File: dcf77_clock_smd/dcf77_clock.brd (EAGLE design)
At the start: 83.5 x 76.2 mm, 42 parts, among them IC1 7805DT, IC2 ATMEGA48/88/168-AU, J2 DCJ0202, Q2 IRLML6244TRPBF, SW1 EC12E_SW, U1 LCD-16X2SILK, U2 DS1307SO8

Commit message: ERC fixes
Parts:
- LED1: value (none) -> BLUE
- Q1: value (none) -> 32.768kHz
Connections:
- removed net N$8: IC2.14
- net LCD_DB6: now also IC2.11; no longer IC2.9
- net LCD_DB7: now also IC2.9; no longer IC2.11
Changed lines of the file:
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@@
 <attribute name="VALUE" x="73.914" y="75.692" size="1.27" layer="27" rot="R270"/>
 </element>
-<element name="LED1" library="led" library_urn="urn:adsk.eagle:library:259" package="CHIP-LED0805" package3d_urn="urn:adsk.eagle:package:15818/2" value="" x="55.88" y="41.91" smashed="yes" rot="R90">
+<element name="LED1" library="led" library_urn="urn:adsk.eagle:library:259" package="CHIP-LED0805" package3d_urn="urn:adsk.eagle:package:15818/2" value="BLUE" x="55.88" y="41.91" smashed="yes" rot="R90">
 <attribute name="NAME" x="55.499" y="43.815" size="1.27" layer="25" ratio="10" rot="R90"/>
 <attribute name="POPULARITY" value="68" x="55.88" y="41.91" size="1.778" layer="27" rot="R90" display="off"/>
@@
 <attribute name="NAME" x="23.45" y="76.5" size="1.27" layer="25"/>
 </element>
-<element name="Q1" library="crystal" library_urn="urn:adsk.eagle:library:204" package="MM39SL" package3d_urn="urn:adsk.eagle:package:12090/1" value="" x="30.48" y="58.42" smashed="yes">
+<element name="Q1" library="crystal" library_urn="urn:adsk.eagle:library:204" package="MM39SL" package3d_urn="urn:adsk.eagle:package:12090/1" value="32.768kHz" x="30.48" y="58.42" smashed="yes">
 <attribute name="MF" value="" x="30.48" y="58.42" size="1.778" layer="27" display="off"/>
 <attribute name="MPN" value="" x="30.48" y="58.42" size="1.778" layer="27" display="off"/>
@@
 <wire x1="41.1226" y1="46.45" x2="47.31" y2="60.96" width="0" layer="19" extent="1-1"/>
 </signal>
-<signal name="N$8">
-<contactref element="IC2" pad="14"/>
-</signal>
 <signal name="ISP_MISO">
 <contactref element="IC2" pad="16"/>
@@
 <signal name="LCD_DB6">
 <contactref element="U1" pad="13"/>
-<contactref element="IC2" pad="9"/>
-<wire x1="40.009" y1="35.058" x2="41.1226" y2="41.65" width="0" layer="19" extent="1-1"/>
+<contactref element="IC2" pad="11"/>
+<wire x1="40.009" y1="35.058" x2="41.1226" y2="43.25" width="0" layer="19" extent="1-1"/>
 </signal>
 <signal name="LCD_DB7">
 <contactref element="U1" pad="14"/>
-<contactref element="IC2" pad="11"/>
-<wire x1="42.549" y1="35.058" x2="41.1226" y2="43.25" width="0" layer="19" extent="1-1"/>
+<contactref element="IC2" pad="9"/>
+<wire x1="42.549" y1="35.058" x2="41.1226" y2="41.65" width="0" layer="19" extent="1-1"/>
 </signal>
 <signal name="N$9">

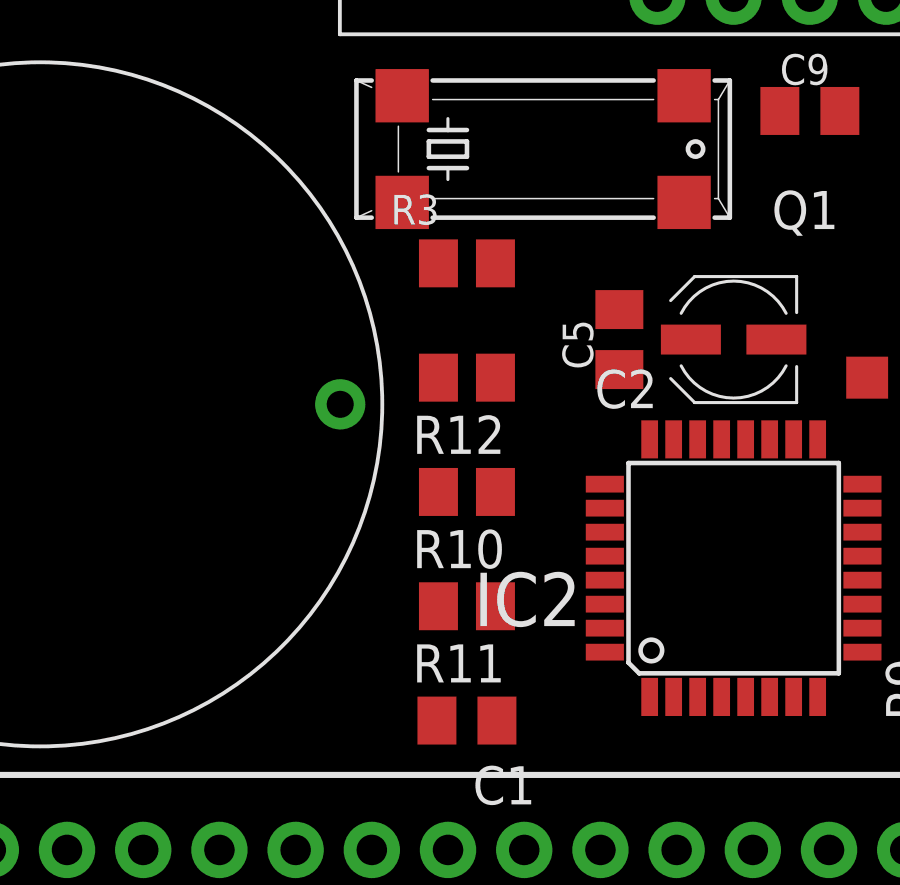
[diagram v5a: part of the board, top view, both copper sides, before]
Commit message: Rearrange I2C pullups
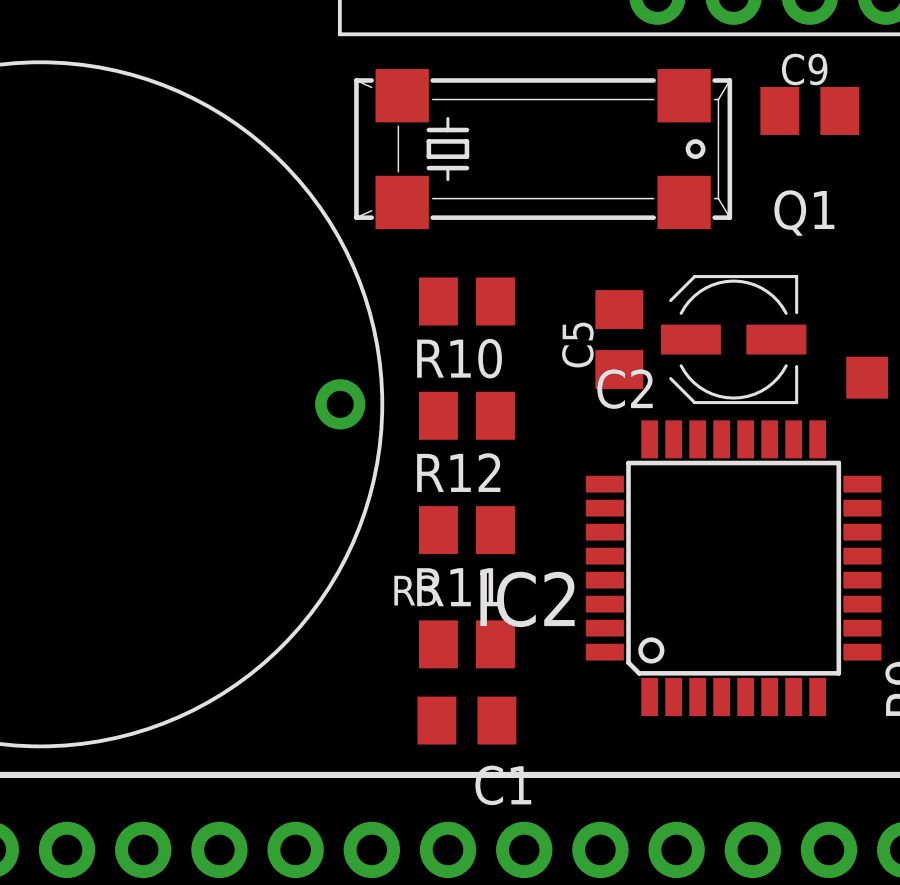
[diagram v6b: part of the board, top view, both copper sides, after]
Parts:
- moved R3 12.7 mm to (27.9, 41.9)
- moved R10 6.35 mm to (27.9, 53.3)
- moved R11 2.54 mm to (27.9, 45.7)
- moved R12 1.27 mm to (27.9, 49.5)
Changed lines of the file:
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@@
 <attribute name="VALUE" x="75.565" y="41.91" size="0.6096" layer="27" rot="R180"/>
 </element>
-<element name="R3" library="rcl" library_urn="urn:adsk.eagle:library:334" package="M0805" package3d_urn="urn:adsk.eagle:package:23556/2" value="10k" x="27.94" y="54.61" smashed="yes">
-<attribute name="NAME" x="25.4" y="55.9054" size="0.9906" layer="25" ratio="10"/>
-<attribute name="POPULARITY" value="45" x="27.94" y="54.61" size="1.778" layer="27" display="off"/>
-<attribute name="SPICEPREFIX" value="R" x="27.94" y="54.61" size="1.778" layer="27" display="off"/>
-<attribute name="VALUE" x="26.3144" y="54.1274" size="0.9906" layer="27" ratio="10"/>
+<element name="R3" library="rcl" library_urn="urn:adsk.eagle:library:334" package="M0805" package3d_urn="urn:adsk.eagle:package:23556/2" value="10k" x="27.94" y="41.91" smashed="yes">
+<attribute name="NAME" x="25.4" y="43.2054" size="0.9906" layer="25" ratio="10"/>
+<attribute name="POPULARITY" value="45" x="27.94" y="41.91" size="1.778" layer="27" display="off"/>
+<attribute name="SPICEPREFIX" value="R" x="27.94" y="41.91" size="1.778" layer="27" display="off"/>
+<attribute name="VALUE" x="26.3144" y="41.4274" size="0.9906" layer="27" ratio="10"/>
 </element>
 <element name="SG2" library="SparkFun" package="BUZZER-CCV-KIT" value="LD-BZEN-1201" x="49.53" y="45.72" smashed="yes">
@@
 <attribute name="VALUE" x="46.99" y="39.37" size="1.27" layer="27" rot="R90"/>
 </element>
-<element name="R10" library="rcl" library_urn="urn:adsk.eagle:library:334" package="M0805" package3d_urn="urn:adsk.eagle:package:23556/2" value="4.7k" x="27.94" y="46.99" smashed="yes" rot="R180">
-<attribute name="NAME" x="29.21" y="45.72" size="1.27" layer="25" rot="R180"/>
-<attribute name="POPULARITY" value="45" x="27.94" y="46.99" size="1.27" layer="27" font="vector" rot="R180" display="off"/>
-<attribute name="SPICEPREFIX" value="R" x="27.94" y="46.99" size="1.27" layer="27" font="vector" rot="R180" display="off"/>
-<attribute name="VALUE" x="29.21" y="49.53" size="1.27" layer="27" rot="R180"/>
-</element>
-<element name="R11" library="rcl" library_urn="urn:adsk.eagle:library:334" package="M0805" package3d_urn="urn:adsk.eagle:package:23556/2" value="4.7k" x="27.94" y="43.18" smashed="yes" rot="R180">
-<attribute name="NAME" x="29.21" y="41.91" size="1.27" layer="25" rot="R180"/>
-<attribute name="POPULARITY" value="45" x="27.94" y="43.18" size="1.27" layer="27" font="vector" rot="R180" display="off"/>
-<attribute name="SPICEPREFIX" value="R" x="27.94" y="43.18" size="1.27" layer="27" font="vector" rot="R180" display="off"/>
-<attribute name="VALUE" x="29.21" y="45.72" size="1.27" layer="27" rot="R180"/>
-</element>
-<element name="R12" library="rcl" library_urn="urn:adsk.eagle:library:334" package="M0805" package3d_urn="urn:adsk.eagle:package:23556/2" value="4.7k" x="27.94" y="50.8" smashed="yes" rot="R180">
-<attribute name="NAME" x="29.21" y="49.53" size="1.27" layer="25" rot="R180"/>
-<attribute name="POPULARITY" value="45" x="27.94" y="50.8" size="1.27" layer="27" font="vector" rot="R180" display="off"/>
-<attribute name="SPICEPREFIX" value="R" x="27.94" y="50.8" size="1.27" layer="27" font="vector" rot="R180" display="off"/>
-<attribute name="VALUE" x="29.21" y="53.34" size="1.27" layer="27" rot="R180"/>
+<element name="R10" library="rcl" library_urn="urn:adsk.eagle:library:334" package="M0805" package3d_urn="urn:adsk.eagle:package:23556/2" value="4.7k" x="27.94" y="53.34" smashed="yes" rot="R180">
+<attribute name="NAME" x="29.21" y="52.07" size="1.27" layer="25" rot="R180"/>
+<attribute name="POPULARITY" value="45" x="27.94" y="53.34" size="1.27" layer="27" font="vector" rot="R180" display="off"/>
+<attribute name="SPICEPREFIX" value="R" x="27.94" y="53.34" size="1.27" layer="27" font="vector" rot="R180" display="off"/>
+<attribute name="VALUE" x="29.21" y="55.88" size="1.27" layer="27" rot="R180"/>
+</element>
+<element name="R11" library="rcl" library_urn="urn:adsk.eagle:library:334" package="M0805" package3d_urn="urn:adsk.eagle:package:23556/2" value="4.7k" x="27.94" y="45.72" smashed="yes" rot="R180">
+<attribute name="NAME" x="29.21" y="44.45" size="1.27" layer="25" rot="R180"/>
+<attribute name="POPULARITY" value="45" x="27.94" y="45.72" size="1.27" layer="27" font="vector" rot="R180" display="off"/>
+<attribute name="SPICEPREFIX" value="R" x="27.94" y="45.72" size="1.27" layer="27" font="vector" rot="R180" display="off"/>
+<attribute name="VALUE" x="29.21" y="48.26" size="1.27" layer="27" rot="R180"/>
+</element>
+<element name="R12" library="rcl" library_urn="urn:adsk.eagle:library:334" package="M0805" package3d_urn="urn:adsk.eagle:package:23556/2" value="4.7k" x="27.94" y="49.53" smashed="yes" rot="R180">
+<attribute name="NAME" x="29.21" y="48.26" size="1.27" layer="25" rot="R180"/>
+<attribute name="POPULARITY" value="45" x="27.94" y="49.53" size="1.27" layer="27" font="vector" rot="R180" display="off"/>
+<attribute name="SPICEPREFIX" value="R" x="27.94" y="49.53" size="1.27" layer="27" font="vector" rot="R180" display="off"/>
+<attribute name="VALUE" x="29.21" y="52.07" size="1.27" layer="27" rot="R180"/>
 </element>
 <element name="C9" library="rcl" library_urn="urn:adsk.eagle:library:334" package="C0805K" package3d_urn="urn:adsk.eagle:package:23681/2" value="100n" x="39.37" y="59.69" smashed="yes">
@@
 <wire x1="35.405" y1="52.07" x2="38.83" y2="48.7426" width="0" layer="19" extent="1-1"/>
 <wire x1="33.02" y1="51.07" x2="35.405" y2="52.07" width="0" layer="19" extent="1-1"/>
-<wire x1="28.89" y1="50.8" x2="33.02" y2="51.07" width="0" layer="19" extent="1-1"/>
-<wire x1="28.89" y1="46.99" x2="28.89" y2="50.8" width="0" layer="19" extent="1-1"/>
-<wire x1="28.89" y1="43.18" x2="28.89" y2="46.99" width="0" layer="19" extent="1-1"/>
-<wire x1="28.94" y1="39.37" x2="28.89" y2="43.18" width="0" layer="19" extent="1-1"/>
-<wire x1="26.99" y1="54.61" x2="28.89" y2="50.8" width="0" layer="19" extent="1-1"/>
+<wire x1="28.89" y1="49.53" x2="33.02" y2="51.07" width="0" layer="19" extent="1-1"/>
+<wire x1="28.89" y1="53.34" x2="28.89" y2="49.53" width="0" layer="19" extent="1-1"/>
+<wire x1="28.89" y1="45.72" x2="28.89" y2="49.53" width="0" layer="19" extent="1-1"/>
+<wire x1="26.99" y1="41.91" x2="28.89" y2="45.72" width="0" layer="19" extent="1-1"/>
+<wire x1="28.94" y1="39.37" x2="26.99" y2="41.91" width="0" layer="19" extent="1-1"/>
 <wire x1="36.43" y1="40.1574" x2="28.94" y2="39.37" width="0" layer="19" extent="1-1"/>
 <wire x1="38.03" y1="40.1574" x2="36.43" y2="40.1574" width="0" layer="19" extent="1-1"/>
@@
 <wire x1="34.29" y1="63.5" x2="38.37" y2="59.69" width="0" layer="19" extent="1-1"/>
 <wire x1="45.089" y1="35.058" x2="38.03" y2="40.1574" width="0" layer="19" extent="1-1"/>
-<wire x1="12.069" y1="35.058" x2="28.94" y2="39.37" width="0" layer="19" extent="1-1"/>
-<wire x1="7.62" y1="64.5" x2="26.99" y2="54.61" width="0" layer="19" extent="1-1"/>
+<wire x1="12.069" y1="35.058" x2="26.99" y2="41.91" width="0" layer="19" extent="1-1"/>
+<wire x1="7.62" y1="64.5" x2="28.89" y2="53.34" width="0" layer="19" extent="1-1"/>
 <wire x1="5.715" y1="60.8838" x2="7.62" y2="64.5" width="0" layer="19" extent="1-1"/>
 </signal>
@@
 <contactref element="R3" pad="2"/>
 <wire x1="32.5374" y1="44.05" x2="77.47" y2="57.15" width="0" layer="19" extent="1-1"/>
-<wire x1="28.89" y1="54.61" x2="32.5374" y2="44.05" width="0" layer="19" extent="1-1"/>
+<wire x1="28.89" y1="41.91" x2="32.5374" y2="44.05" width="0" layer="19" extent="1-1"/>
 </signal>
 <signal name="ISP_MOSI_BUZ_PWM">
@@
 <contactref element="R10" pad="2"/>
 <contactref element="IC2" pad="26"/>
-<wire x1="26.99" y1="46.99" x2="32.5374" y2="46.45" width="0" layer="19" extent="1-1"/>
-<wire x1="4.445" y1="60.8838" x2="26.99" y2="46.99" width="0" layer="19" extent="1-1"/>
+<wire x1="32.5374" y1="46.45" x2="26.99" y2="53.34" width="0" layer="19" extent="1-1"/>
+<wire x1="4.445" y1="60.8838" x2="26.99" y2="53.34" width="0" layer="19" extent="1-1"/>
 </signal>
 <signal name="RTC_SCL">
@@
 <contactref element="R11" pad="2"/>
 <contactref element="IC2" pad="28"/>
-<wire x1="26.99" y1="43.18" x2="32.5374" y2="44.85" width="0" layer="19" extent="1-1"/>
-<wire x1="3.175" y1="60.8838" x2="26.99" y2="43.18" width="0" layer="19" extent="1-1"/>
+<wire x1="26.99" y1="45.72" x2="32.5374" y2="44.85" width="0" layer="19" extent="1-1"/>
+<wire x1="3.175" y1="60.8838" x2="26.99" y2="45.72" width="0" layer="19" extent="1-1"/>
 </signal>
 <signal name="RTC_SDA">
@@
 <contactref element="R12" pad="2"/>
 <contactref element="IC2" pad="27"/>
-<wire x1="32.5374" y1="45.65" x2="26.99" y2="50.8" width="0" layer="19" extent="1-1"/>
-<wire x1="1.905" y1="60.8838" x2="26.99" y2="50.8" width="0" layer="19" extent="1-1"/>
+<wire x1="32.5374" y1="45.65" x2="26.99" y2="49.53" width="0" layer="19" extent="1-1"/>
+<wire x1="1.905" y1="60.8838" x2="26.99" y2="49.53" width="0" layer="19" extent="1-1"/>
 </signal>
 </signals>

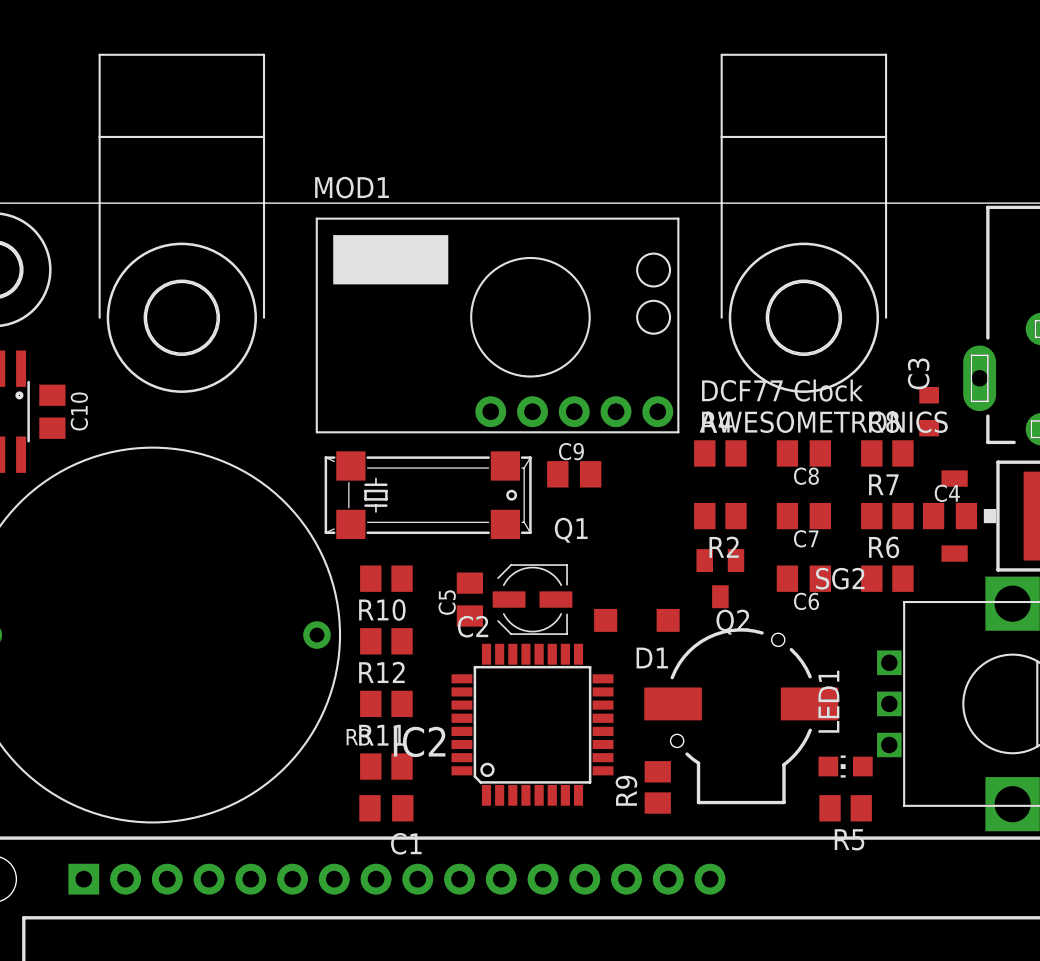
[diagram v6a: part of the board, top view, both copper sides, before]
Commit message: Change buzzer footprint
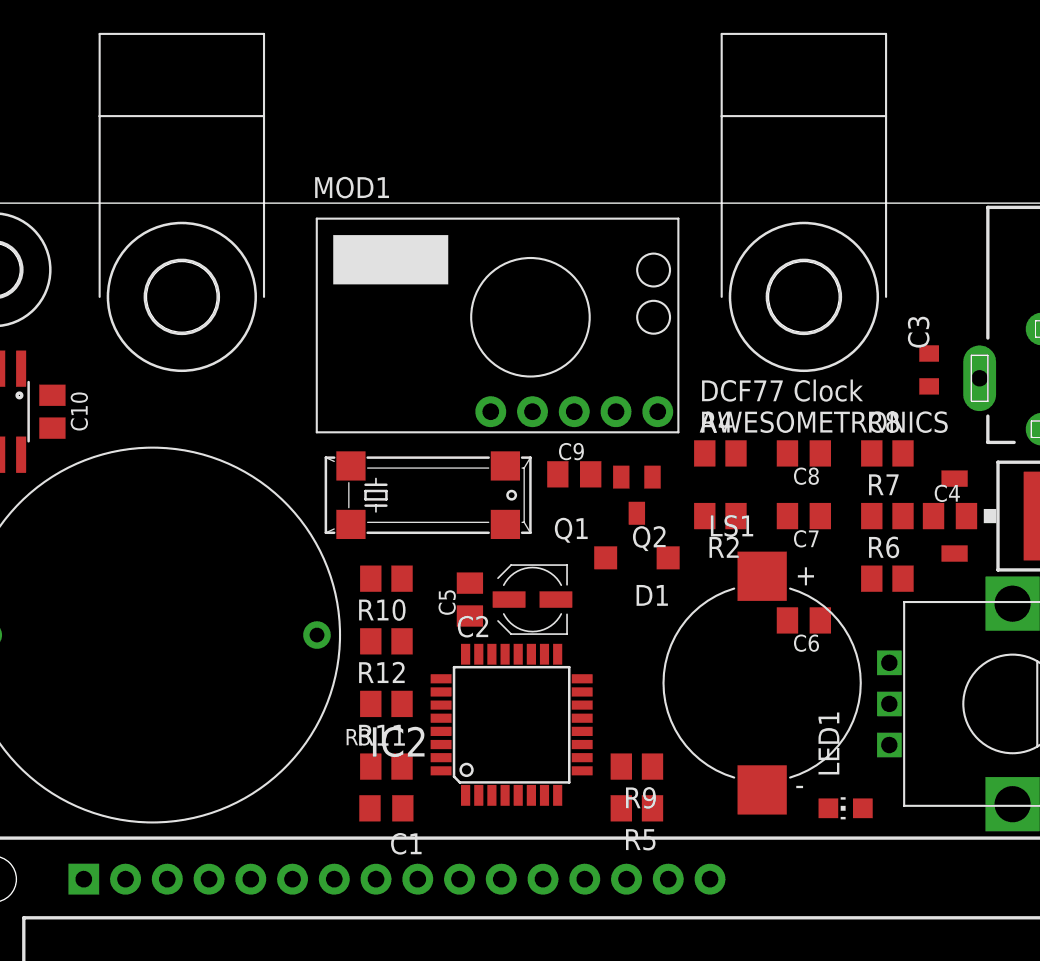
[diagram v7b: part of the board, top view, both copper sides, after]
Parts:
- removed SG2: LD-BZEN-1201, SparkFun:BUZZER-CCV-KIT
- added LS1: CD-1206-SMT, CD-1206-SMT:CUI_CD-1206-SMT
- moved R5 12.7 mm to (43.2, 39.4)
- moved Q2 7.18 mm to (43.2, 58.4)
- moved D1 3.81 mm to (43.2, 54.6)
- moved C3 2.54 mm to (61.0, 66.0)
- moved C6 2.54 mm to (53.3, 50.8)
- moved LED1 2.54 mm to (55.9, 39.4)
- moved R9 1.80 mm to (43.2, 41.9), turned to 180 degrees
- moved HOLD1 1.27 mm to (15.5, 70.5)
- moved HOLD2 1.27 mm to (53.3, 70.5)
- moved IC2 1.27 mm to (35.6, 44.5)
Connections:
- net N$2: now also LS1.M; no longer SG2.-
- net VCC: now also LS1.P; no longer SG2.+
